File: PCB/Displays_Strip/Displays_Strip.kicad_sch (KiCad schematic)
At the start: 25 parts, among them J1 Power, J2 ICSP, J3 Comm_I2C, J4 EEPROM_Prog, U1 PIC32MX270F256D-IPT, U15 M95P32-IXMGT/E, U16 LDL1117S33R, Y1 16M

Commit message: Schematic Flash
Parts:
- added C11, C12: 100n, Capacitor_SMD:C_0805_2012Metric, symbol Device:C
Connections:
- net +3.3V: now also J4.1 (Pin_1), C11.1, C12.1; no longer J4.3 (Pin_3)
- net CLK_MEM: now also J4.3 (Pin_3); no longer J4.5 (Pin_5)
- net GND: now also C11.2, C12.2
- net MISO_MEM: now also J4.6 (Pin_6); no longer J4.1 (Pin_1)
- net MOSI_MEM: now also J4.4 (Pin_4); no longer J4.6 (Pin_6)
- net nCS_MEM: now also J4.5 (Pin_5); no longer J4.2 (Pin_2)
- net nHOLD_MEM: now also J4.2 (Pin_2); no longer J4.4 (Pin_4)
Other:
- moved on the sheet: C4, C5, C8

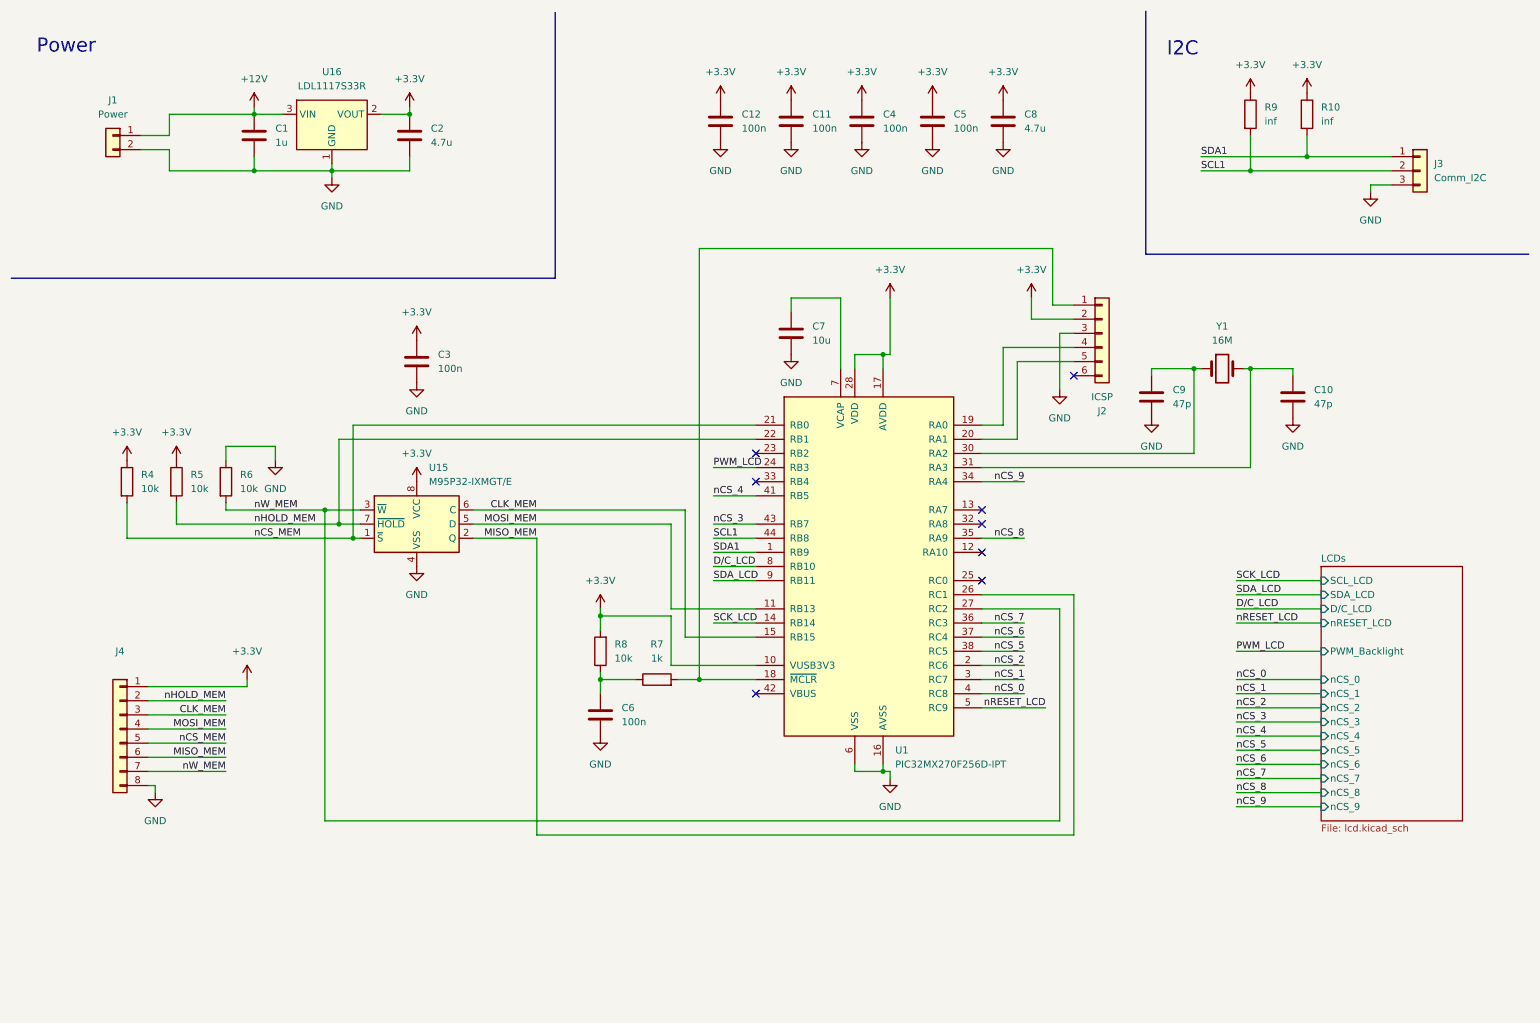
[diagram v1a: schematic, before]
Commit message: PCB Displays
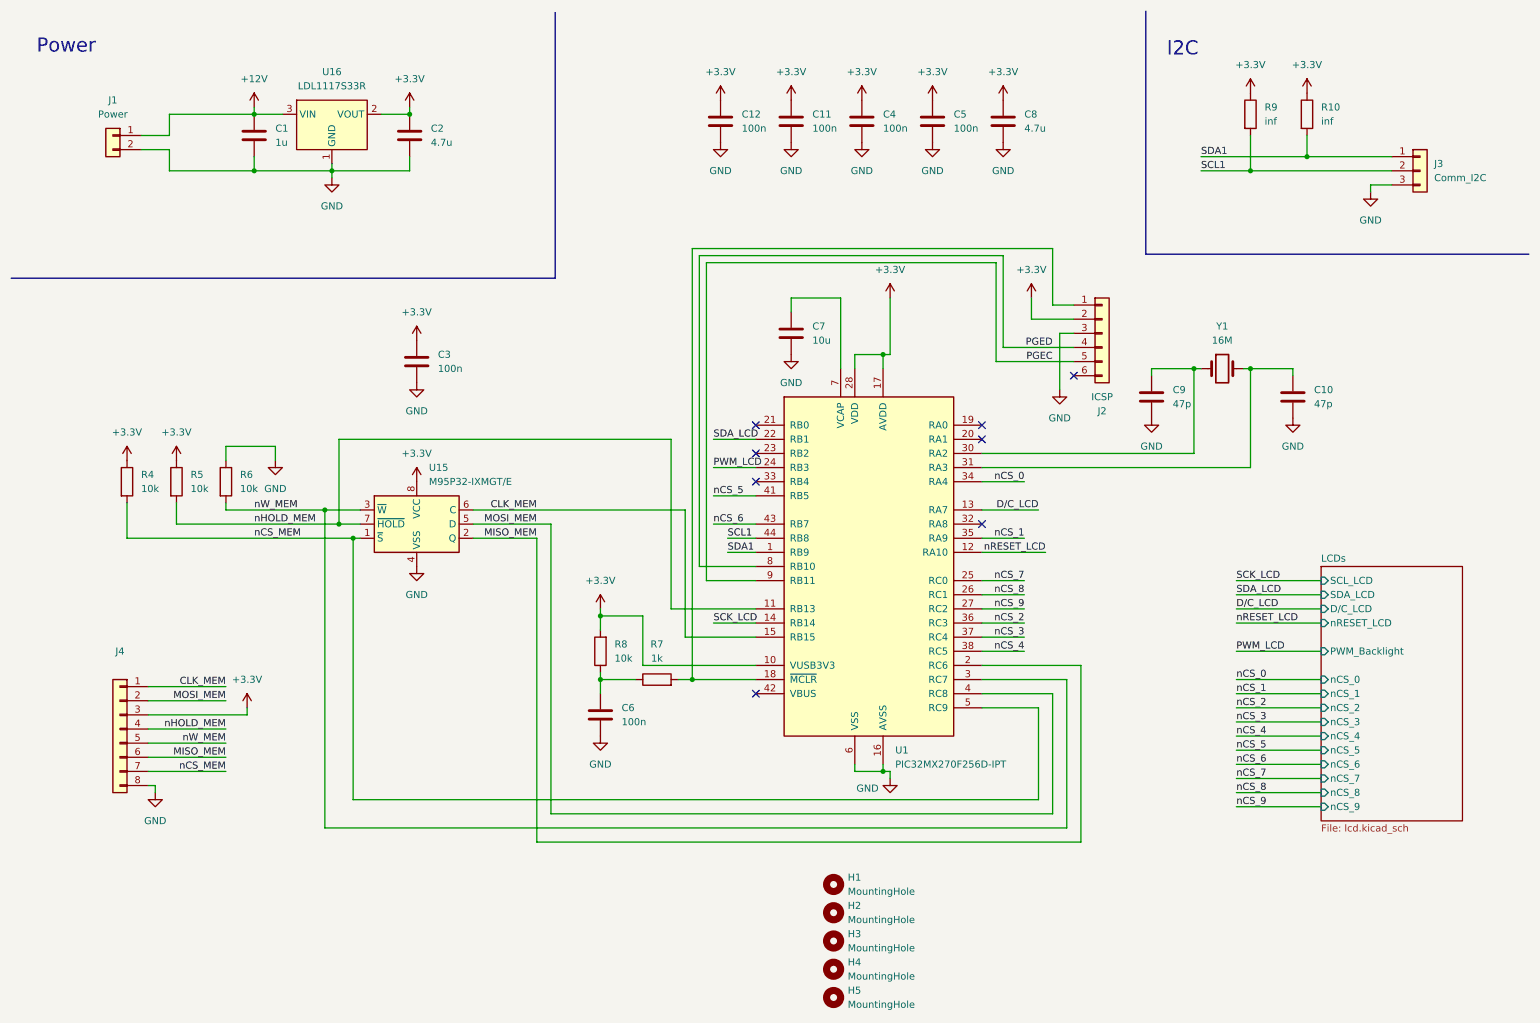
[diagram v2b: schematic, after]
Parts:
- added H1, H2, H3, H4, H5: MountingHole, MountingHole:MountingHole_3.2mm_M3, symbol Mechanical:MountingHole
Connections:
- net +3.3V: now also J4.3 (Pin_3); no longer J4.1 (Pin_1)
- net CLK_MEM: now also J4.1 (Pin_1); no longer J4.3 (Pin_3)
- net D/C_LCD: now also U1.13 (RA7); no longer U1.8 (RB10)
- net MISO_MEM: now also U1.2 (RC6); no longer U1.26 (RC1)
- net MOSI_MEM: now also J4.2 (Pin_2), U1.4 (RC8); no longer J4.4 (Pin_4), U1.11 (RB13)
- net SDA_LCD: now also U1.22 (RB1); no longer U1.9 (RB11)
- net nCS_0: now also U1.34 (RA4); no longer U1.4 (RC8)
- net nCS_1: now also U1.35 (RA9); no longer U1.3 (RC7)
- net nCS_2: now also U1.36 (RC3); no longer U1.2 (RC6)
- net nCS_3: now also U1.37 (RC4); no longer U1.43 (RB7)
- net nCS_4: now also U1.38 (RC5); no longer U1.41 (RB5)
- net nCS_5: now also U1.41 (RB5); no longer U1.38 (RC5)
- net nCS_6: now also U1.43 (RB7); no longer U1.37 (RC4)
- net nCS_7: now also U1.25 (RC0); no longer U1.36 (RC3)
- net nCS_8: now also U1.26 (RC1); no longer U1.35 (RA9)
- net nCS_9: now also U1.27 (RC2); no longer U1.34 (RA4)
- net nCS_MEM: now also J4.7 (Pin_7), U1.5 (RC9); no longer J4.5 (Pin_5), U1.21 (RB0)
- net nHOLD_MEM: now also J4.4 (Pin_4), U1.11 (RB13); no longer J4.2 (Pin_2), U1.22 (RB1)
- net nRESET_LCD: now also U1.12 (RA10); no longer U1.5 (RC9)
- net nW_MEM: now also J4.5 (Pin_5), U1.3 (RC7); no longer J4.7 (Pin_7), U1.27 (RC2)
- net at U1.19 (RA0): no longer J2.4 (Pin_4)
- net at U1.20 (RA1): no longer J2.5 (Pin_5)
- new net PGEC: J2.5 (Pin_5), U1.9 (RB11)
- new net PGED: J2.4 (Pin_4), U1.8 (RB10)
